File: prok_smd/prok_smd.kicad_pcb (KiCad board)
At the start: 2 copper layers, 105 x 41.2 mm, 60 parts, among them CON1 microSD_Card, J1 POWER, J10 Conn_01x02_Female, J11 Conn_01x02_Female, J12 Conn_01x05_Male, J13 Conn_01x02_Female, J14 Conn_01x02_Female, J15 Conn_01x02_Male, J16 Conn_01x02_Male, J17 Conn_01x02_Male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

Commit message: :sparkles: :construction: first draft v2 board
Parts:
- removed J10, J11, J13, J14: Conn_01x02_Female, Connector_PinSocket_2.54mm:PinSocket_1x02_P2.54mm_Vertical
- removed J15, J16, J18: Conn_01x02_Male, Connector_PinHeader_2.54mm:PinHeader_1x02_P2.54mm_Vertical
- added J2: Conn_01x03_Female, Connector_PinSocket_2.54mm:PinSocket_1x03_P2.54mm_Vertical_SMD_Pin1Left, B.Cu at (104.0, 59.9)
- J17: value Conn_01x02_Male -> Conn_01x03_Male; footprint Connector_PinHeader_2.54mm:PinHeader_1x02_P2.54mm_Vertical -> Connector_PinHeader_2.54mm:PinHeader_1x03_P2.54mm_Vertical
- J9: footprint Connector_PinSocket_2.54mm:PinSocket_1x05_P2.54mm_Vertical -> Connector_PinSocket_2.54mm:PinSocket_1x05_P2.54mm_Vertical_SMD_Pin1Left
- moved mouse-bite-2mm-slot 100.9 mm to (102.1, 53.9), turned to 180 degrees
- moved J17 81.9 mm to (104.0, 40.7), turned to 180 degrees
- moved D1 78.9 mm to (109.1, 35.9), turned to 180 degrees
- moved R5 75.6 mm to (177.6, 60.0), turned to 270 degrees
- moved R10 74.6 mm to (179.5, 69.0), turned to 90 degrees
- moved C4 74.4 mm to (112.8, 35.9), turned to 270 degrees
- moved R18 73.1 mm to (174.3, 59.5), turned to 180 degrees
- moved J1 72.8 mm to (119.0, 39.8), turned to 270 degrees
- moved C5 72.4 mm to (114.6, 35.9), turned to 90 degrees
- moved R7 71.6 mm to (192.3, 68.0)
- moved R9 71.6 mm to (192.3, 69.7)
- moved R4 70.7 mm to (178.0, 65.2), turned to 270 degrees
- moved D2 68.8 mm to (118.6, 36.0)
- moved U1 68.7 mm to (186.8, 64.8), turned to 180 degrees
- moved U3 67.5 mm to (174.8, 65.2), turned to 90 degrees
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- renumbered CHANNEL to CHANNEL1, EXPAND to EXPAND1, TIME to TIME1
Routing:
- net +12V: track 101.9 -> 0.00 mm, vias 7 -> 4
- net LED_1: track 100.8 -> 0.00 mm, vias 1 -> 0
- net LED_2: track 100.2 -> 0.00 mm, vias 1 -> 0
- net GND: track 97.4 -> 0.00 mm, vias 11 -> 4
- net +3V3: track 96.9 -> 0.00 mm, vias 4 -> 0
- net -12V: track 94.3 -> 0.00 mm, vias 3 -> 0
- net LED_4: track 91.7 -> 0.00 mm, vias 1 -> 0
- net +5V: track 91.6 -> 0.00 mm, vias 1 -> 0
- net LED_3: track 88.9 -> 0.00 mm, vias 1 -> 0
- net CHANNEL_POT: track 81.6 -> 0.00 mm, vias 2 -> 0
- net TIME_POT: track 50.0 -> 0.00 mm, vias 6 -> 0
- net A4: track 36.7 -> 0.00 mm
- net A5: track 36.4 -> 0.00 mm
- net RESET_CV: track 33.0 -> 0.00 mm, vias 1 -> 0
- net MISO: track 30.0 -> 0.00 mm, vias 2 -> 0
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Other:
- outline, holes or cut-outs redrawn

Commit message: :sparkles: :construction: first draft routing v2
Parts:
- moved R2 5.91 mm to (172.1, 67.0)
- moved R1 5.88 mm to (170.6, 67.0), turned to 270 degrees
- moved R16 3.59 mm to (199.1, 69.6)
- moved R14 3.51 mm to (201.1, 69.6)
- moved R13 3.50 mm to (201.0, 60.4)
- moved R15 3.47 mm to (199.0, 60.4)
- moved R10 2.82 mm to (176.9, 70.2), turned to 180 degrees
- moved R11 2.03 mm to (180.0, 70.2)
- moved EXPAND1 1.41 mm to (152.0, 56.9)
- moved R17 0.51 mm to (143.4, 68.1)
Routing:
- net +5V: track 0.00 -> 88.5 mm
- net +3V3: track 0.00 -> 85.1 mm, vias 0 -> 2
- net +12V: track 0.00 -> 83.7 mm, vias 4 -> 6
- net Net-(J7-PadT): track 0.00 -> 80.4 mm, vias 0 -> 1
- net Net-(J6-PadT): track 0.00 -> 79.8 mm, vias 0 -> 3
- net Net-(J8-PadT): track 0.00 -> 78.4 mm, vias 0 -> 3
- net -12V: track 0.00 -> 76.9 mm
- net Net-(J5-PadT): track 0.00 -> 75.2 mm, vias 0 -> 1
- net MOSI: track 0.00 -> 50.1 mm
- net RESET_SW: track 0.00 -> 50.0 mm
- net MISO: track 0.00 -> 50.0 mm
- net SCLK: track 0.00 -> 50.0 mm
- net SS: track 0.00 -> 50.0 mm
- net TIME_POT: track 0.00 -> 40.6 mm
- net LED_RESET: track 0.00 -> 37.1 mm, vias 0 -> 1
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
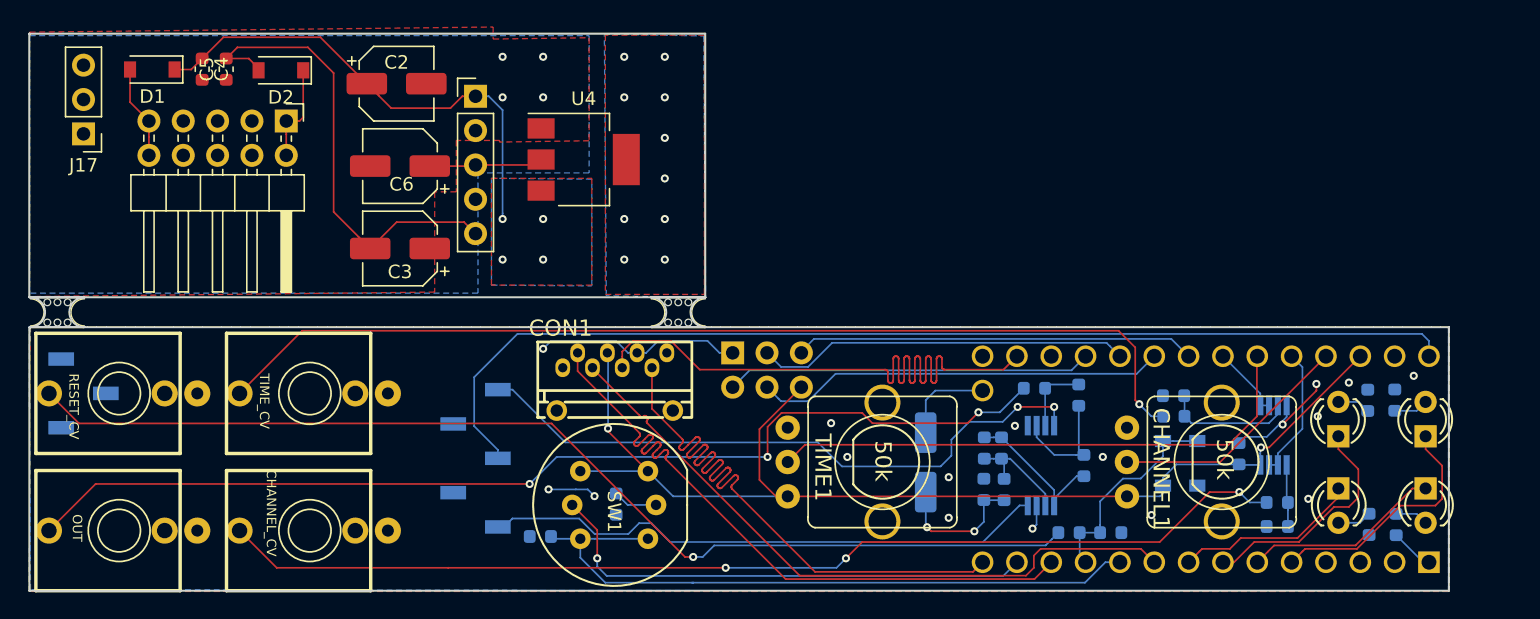
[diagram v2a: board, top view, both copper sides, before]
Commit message: :sparkles: Silkscreen cleanup
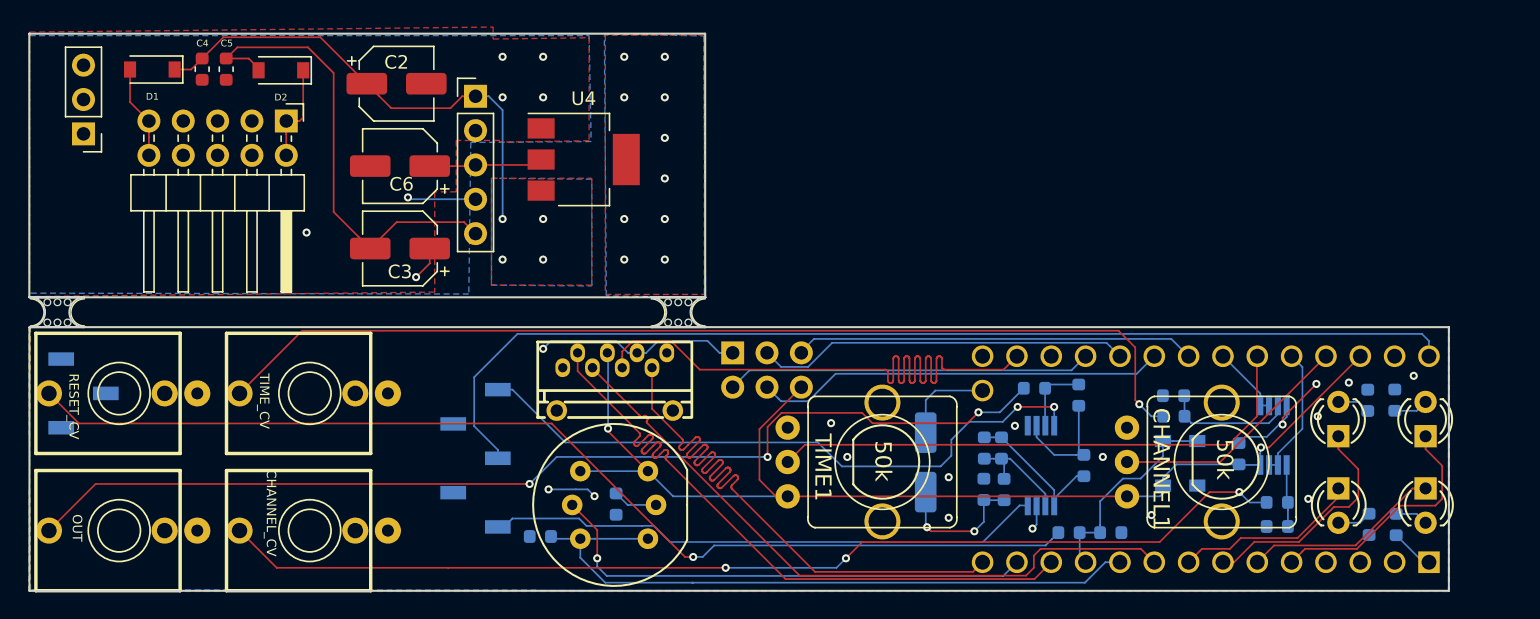
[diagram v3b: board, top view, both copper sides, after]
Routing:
- net GND: track 33.3 -> 40.9 mm, vias 21 -> 24
- net -12V: track 76.9 -> 76.3 mm

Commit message: :sparkles: Clarify silkscreen LEDs, thicken power traces
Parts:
- D5, D6, D7, D8: footprint 4ms-footprints:LED-3MM-SQUARE-ANODE -> prok_smd:LED-3MM-SQUARE-ANODE
- moved R3 0.21 mm to (172.1, 63.9)
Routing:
- net Net-(C8-Pad2): track 11.3 -> 12.6 mm
- net +12V: track 83.7 -> 83.1 mm
- net +3V3: track 85.1 -> 85.7 mm

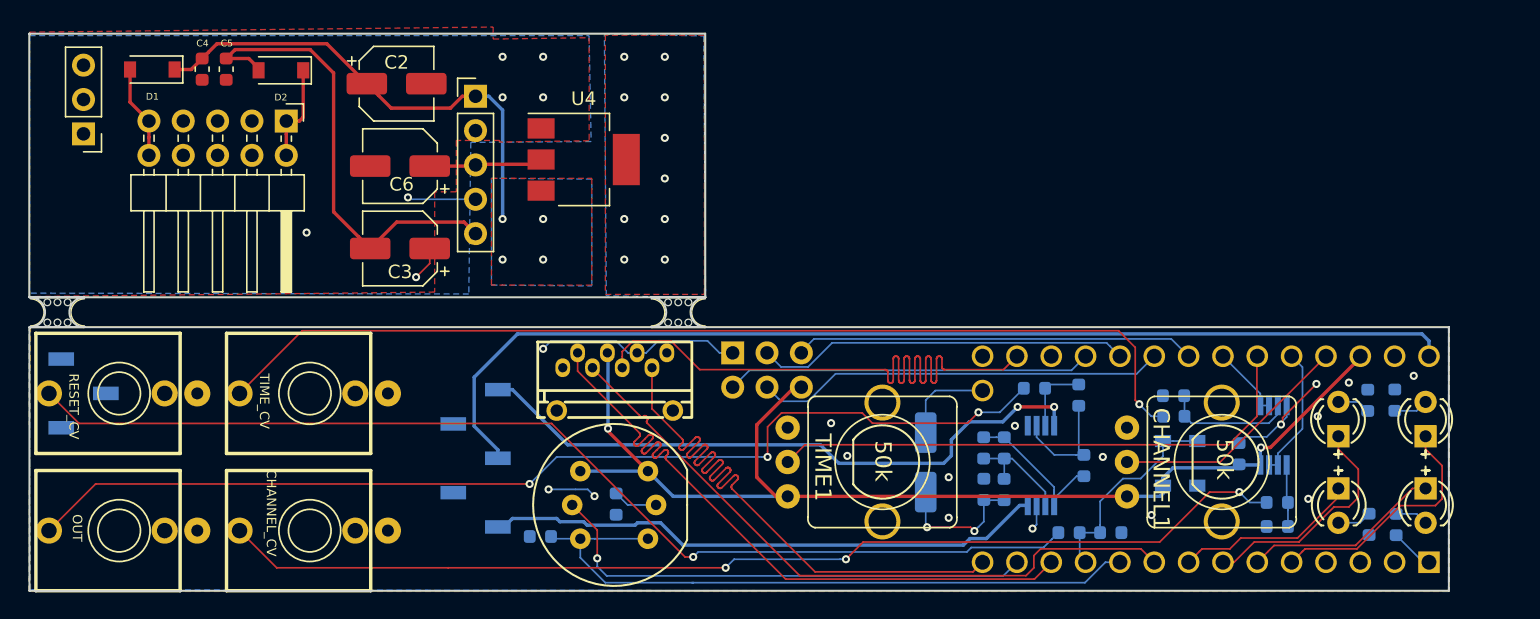
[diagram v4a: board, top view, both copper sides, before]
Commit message: :lipstick: :sparkles: Gold (soldermask hole) instead of silkscreen
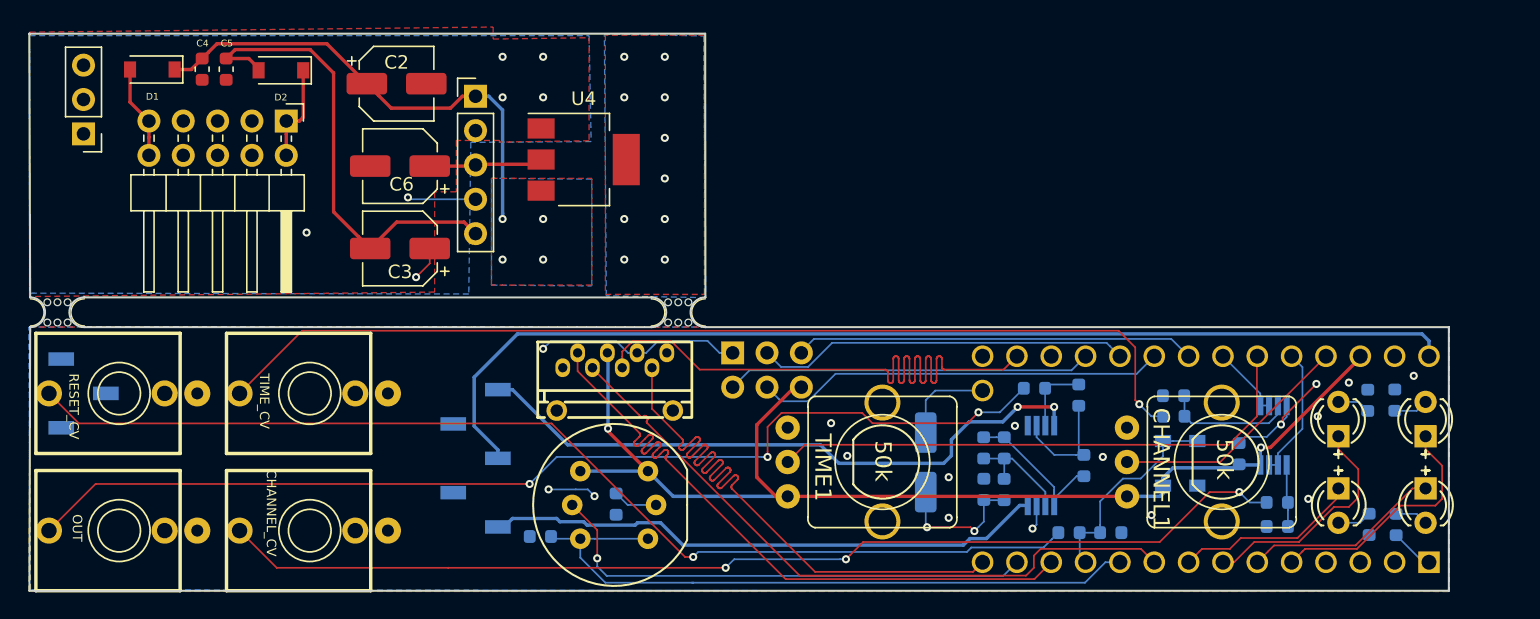
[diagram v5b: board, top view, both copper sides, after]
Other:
- outline, holes or cut-outs redrawn
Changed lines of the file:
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@@
-(kicad_pcb (version 20171130) (host pcbnew "(5.0.2)-1")
+(kicad_pcb (version 20171130) (host pcbnew 5.1.2)
   (general
     (thickness 1.6)
-    (drawings 52)
+    (drawings 49)
     (tracks 905)
     (zones 0)
@@
     (zone_45_only no)
     (trace_min 0.127)
-    (segment_width 0.2)
-    (edge_width 0.15)
     (via_size 0.6)
     (via_drill 0.3)
@@
     (uvia_min_size 0.2)
     (uvia_min_drill 0.1)
+    (edge_width 0.15)
+    (segment_width 0.2)
     (pcb_text_width 0.3)
     (pcb_text_size 1.5 1.5)
@@
     (visible_elements 7FFFFFFF)
     (pcbplotparams
-      (layerselection 0x010fc_ffffffff)
+      (layerselection 0x010f0_ffffffff)
       (usegerberextensions false)
       (usegerberattributes false)
@@
       (outputformat 1)
       (mirror false)
-      (drillshape 1)
+      (drillshape 0)
       (scaleselection 1)
-      (outputdirectory ""))
+      (outputdirectory "gerber/"))
   )
   (net 0 "")
@@
     (uvia_dia 0.3)
     (uvia_drill 0.1)
+    (diff_pair_width 0.127)
     (diff_pair_gap 0.127)
-    (diff_pair_width 0.127)
     (add_net +12V)
     (add_net +3V3)
@@
     )
   )
+  (gr_line (start 100.054 52.7976) (end 99.988 33.2899) (layer Edge.Cuts) (width 0.15))
+  (gr_line (start 100.054 54.9976) (end 100 74.5) (layer Edge.Cuts) (width 0.15))
+  (gr_line (start 150.004 52.7991) (end 149.988 33.2899) (layer Edge.Cuts) (width 0.15))
+  (gr_line (start 150.004 54.9991) (end 205 55) (layer Edge.Cuts) (width 0.15))
+  (gr_line (start 104.054 54.9976) (end 146.004 54.9991) (layer Edge.Cuts) (width 0.15))
+  (gr_line (start 104.054 52.7976) (end 146.004 52.7991) (layer Edge.Cuts) (width 0.15))
   (gr_circle (center 190.7 61.9) (end 190.8 61.9) (layer B.SilkS) (width 0.2))
   (gr_circle (center 175.7 66.6) (end 175.8 66.6) (layer B.SilkS) (width 0.2))
-  (gr_line (start 150.004 52.7991) (end 146.004 52.7991) (layer Edge.Cuts) (width 0.15))
-  (gr_line (start 146.004 54.9991) (end 150.004 54.9991) (layer Edge.Cuts) (width 0.15))
   (gr_arc (start 150.004 53.8991) (end 150.004 52.7991) (angle -180) (layer Edge.Cuts) (width 0.15))
   (gr_arc (start 146.004 53.8991) (end 146.004 54.9991) (angle -180) (layer Edge.Cuts) (width 0.15))
   (gr_arc (start 100.054 53.8976) (end 100.054 54.9976) (angle -180) (layer Edge.Cuts) (width 0.15))
   (gr_arc (start 104.054 53.8976) (end 104.054 52.7976) (angle -180) (layer Edge.Cuts) (width 0.15))
-  (gr_line (start 100.054 54.9976) (end 104.054 54.9976) (layer Edge.Cuts) (width 0.15))
-  (gr_line (start 104.054 52.7976) (end 100.054 52.7976) (layer Edge.Cuts) (width 0.15))
   (gr_line (start 196.825 67.35) (end 196.825 61.425) (layer Dwgs.User) (width 0.2))
   (gr_line (start 205 61.8) (end 194.7 61.8) (layer Dwgs.User) (width 0.2))
@@
     (arrow2b (pts (xy 218.166281 52.8) (xy 217.57986 51.673496)))
   )
-  (gr_line (start 149.988 52.7899) (end 149.988 33.2899) (layer Edge.Cuts) (width 0.15))
-  (gr_line (start 99.988 52.7899) (end 149.988 52.7899) (layer Edge.Cuts) (width 0.15))
-  (gr_line (start 99.988 33.2899) (end 99.988 52.7899) (layer Edge.Cuts) (width 0.15))
-  (gr_line (start 205 55) (end 100 55) (layer Edge.Cuts) (width 0.15))
   (gr_line (start 205 74.5) (end 205 55) (layer Edge.Cuts) (width 0.15))
   (gr_line (start 100 74.5) (end 205 74.5) (layer Edge.Cuts) (width 0.15))
-  (gr_line (start 100 55) (end 100 74.5) (layer Edge.Cuts) (width 0.15))
   (dimension 105 (width 0.3) (layer Dwgs.User)
     (gr_text "105,000 mm" (at 152.40159 97.261112) (layer Dwgs.User)

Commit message: :bug: Fix LEDs misplacement
Led pads were placed 2.5mm lower than they should have.
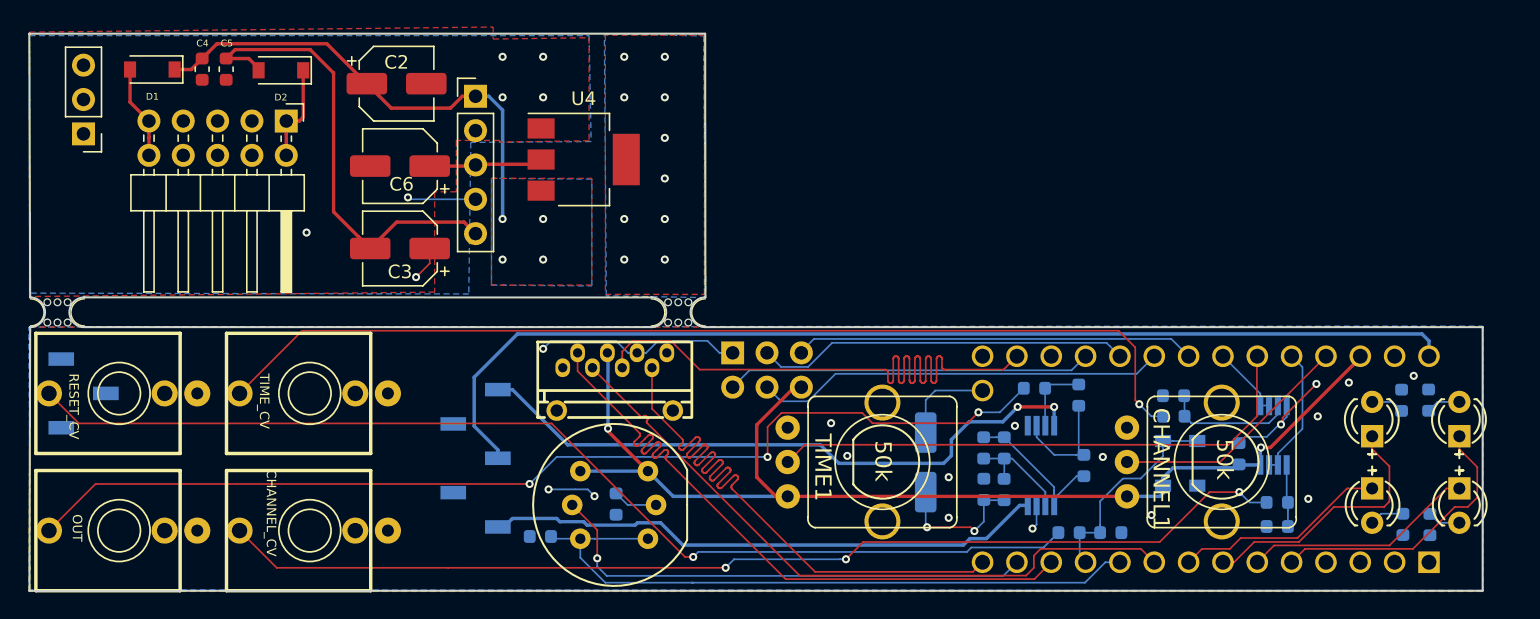
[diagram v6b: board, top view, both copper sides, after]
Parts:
- moved D5 2.50 mm to (205.8, 61.8)
- moved D6 2.50 mm to (205.8, 68.2)
- moved D7 2.50 mm to (199.3, 61.8)
- moved D8 2.50 mm to (199.3, 68.2)
- moved R13 2.50 mm to (203.5, 60.4)
- moved R14 2.50 mm to (203.6, 69.6)
- moved R15 2.50 mm to (201.5, 60.4)
- moved R16 2.50 mm to (201.6, 69.6)
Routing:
- net GND: track 40.9 -> 37.6 mm
- net LED_1: track 18.2 -> 20.8 mm
- net LED_2: track 14.7 -> 17.2 mm
- net LED_3: track 17.1 -> 19.5 mm
- net LED_4: track 13.7 -> 15.8 mm
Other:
- board size 105 x 41.2 mm -> 107.5 x 41.2 mm

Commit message: :recycle: redid power pcb single
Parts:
- removed mouse-bite-2mm-slot (x2): VAL**, Panelization:mouse-bite-2mm-slot
- C4, C5: moved to B.Cu
- D5, D6, D7, D8: footprint prok_smd:LED-3MM-SQUARE-ANODE -> 4ms-footprints:LED-3MM-SQUARE-ANODE
- J17: value Conn_01x03_Male -> Conn_01x05_Male; footprint Connector_PinHeader_2.54mm:PinHeader_1x03_P2.54mm_Vertical -> Connector_PinHeader_2.54mm:PinHeader_1x05_P2.54mm_Vertical
- J2: value Conn_01x03_Female -> Conn_01x05_Female; footprint Connector_PinSocket_2.54mm:PinSocket_1x03_P2.54mm_Vertical_SMD_Pin1Left -> Connector_PinSocket_2.54mm:PinSocket_1x05_P2.54mm_Vertical_SMD_Pin1Left
- moved C5 35.4 mm to (130.5, 67.5), turned to 180 degrees
- moved C4 30.7 mm to (130.5, 61.0), turned to 180 degrees
- moved J17 7.56 mm to (104.0, 48.3)
- moved D2 5.45 mm to (124.0, 36.8), turned to 270 degrees
- moved J2 5.12 mm to (104.0, 65.0), turned to 180 degrees
- moved J1 4.54 mm to (120.7, 35.6)
- moved U4 3.50 mm to (144.5, 42.6)
- moved C2 2.54 mm to (129.7, 37.0)
- moved C3 2.38 mm to (129.8, 49.2)
- moved J9 2.35 mm to (135.3, 64.7), turned to 0 degrees
- moved C6 2.34 mm to (129.7, 43.1)
- moved J12 2.33 mm to (135.3, 37.9)
- moved D1 1.79 mm to (107.5, 36.8), turned to 270 degrees
- moved R12 0.78 mm to (138.4, 70.1), turned to 90 degrees
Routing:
- net Net-(J8-PadT): track 78.4 -> 27.9 mm, vias 3 -> 2
- net -12V: track 76.5 -> 29.1 mm
- net +12V: track 83.1 -> 40.4 mm, vias 6 -> 5
- net GND: track 37.6 -> 22.4 mm, vias 24 -> 6
- net +5V: track 88.5 -> 73.7 mm
- net Net-(D2-Pad1): track 7.38 -> 0.00 mm
- net Net-(D1-Pad2): track 6.93 -> 0.00 mm
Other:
- outline, holes or cut-outs redrawn

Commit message: :recycle: rerouted all pcb
same


same
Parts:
- moved R9 6.05 mm to (194.8, 64.2), turned to 270 degrees
- moved R12 4.94 mm to (143.2, 68.8), turned to 180 degrees
- moved U4 1.75 mm to (142.8, 42.6)
- moved C5 1.46 mm to (130.5, 69.0), turned to 270 degrees
- moved R17 0.86 mm to (143.2, 67.2), turned to 0 degrees
- turned C4 to 270 degrees
- turned J9 to 180 degrees
- renumbered CHANNEL1 to X, TIME1 to Y
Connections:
- J12 pad 2: GND -> Net-(J12-Pad2)
- J12 pad 4: GND -> Net-(J12-Pad4)
- J9 pad 2: GND -> Net-(J9-Pad2)
- J9 pad 4: GND -> Net-(J9-Pad4)
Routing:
- net GND: track 22.4 -> 196.9 mm, vias 6 -> 13
- net +12V: track 40.4 -> 105.7 mm, vias 5 -> 6
- net Net-(J8-PadT): track 27.9 -> 83.5 mm, vias 2 -> 3
- net -12V: track 29.1 -> 77.5 mm
- net +5V: track 73.7 -> 88.8 mm, vias 0 -> 2
- net Net-(D2-Pad1): track 0.00 -> 6.06 mm
- net Net-(D1-Pad2): track 0.00 -> 5.75 mm
- net Net-(J7-PadT): track 80.4 -> 85.6 mm, vias 1 -> 5
- net CHANNEL_POT: track 18.0 -> 22.5 mm, vias 0 -> 1
- net +3V3: track 85.7 -> 89.2 mm, vias 2 -> 3
- net A4: track 30.5 -> 33.3 mm, vias 0 -> 2
- net CHANNEL_CV: track 4.59 -> 6.72 mm
- net A5: track 29.7 -> 31.6 mm, vias 0 -> 2
- net A2: track 27.1 -> 28.5 mm
- net RESET_SW: track 50.2 -> 51.3 mm, vias 0 -> 1
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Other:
- board size 107.5 x 41.2 mm -> 107.5 x 41.3 mm
- board text added: "+"
